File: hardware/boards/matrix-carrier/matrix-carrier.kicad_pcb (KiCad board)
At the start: 2 copper layers, 46.4 x 42 mm, 6 parts, among them J1 2x12 1.27mm shrouded box head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, J2 1x10 2.54mm pin header, SMD, J3 1x10 2.54mm pin header, SMD

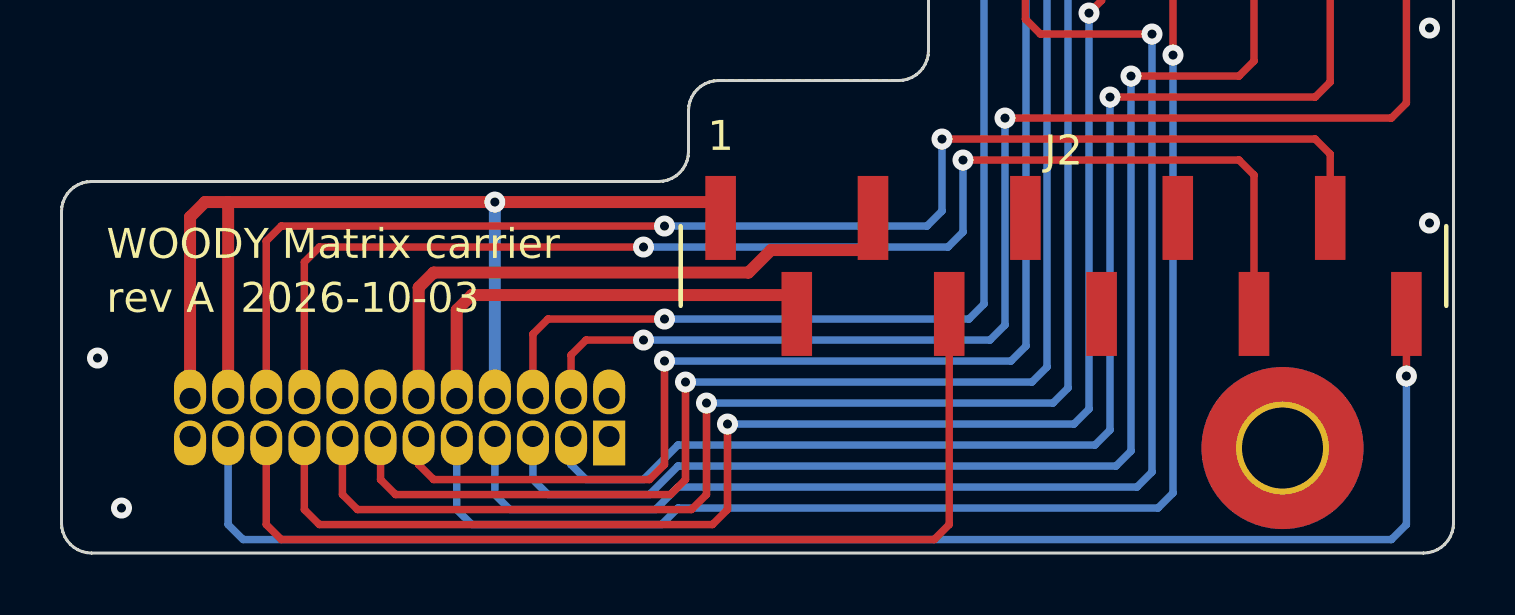
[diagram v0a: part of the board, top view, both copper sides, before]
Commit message: Clash fixes: the Matrix's underside parts drawn at their depth over the carrier (the receptacle is its own solid); the carrier's arm stops short of the right-hand key board's tail end. Carrier re-made on the new outline, check 0 errors, rendered (#23)
Gate-Red: WIP - CAD outputs and clash rebuilding after the scad fix

Co-Authored-By: Claude Opus 5.5 <noreply@anthropic.com>
Claude-Session: https://claude.ai/code/session_01LmB4muFXnoLprWX4JzuJ5A
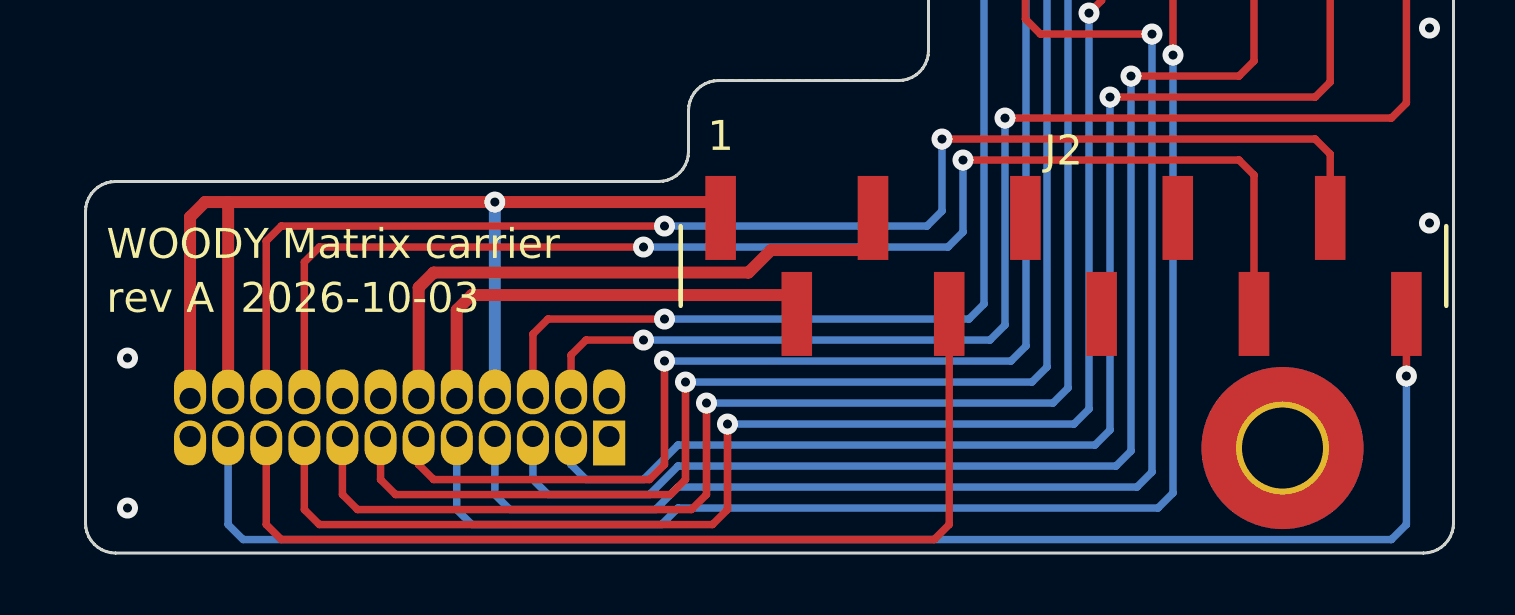
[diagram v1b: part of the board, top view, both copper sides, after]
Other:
- board size 46.4 x 42 mm -> 45.6 x 42 mm

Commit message: #37: MIDI out circuit, the ribbon's MIDI pair, carrier re-route, ADR 0015 amendment
- hardware/carrier/midi-out/: new circuit (sheet, netlist, BOM, page): CA-033's 5 V row
  from U-LVLSHIFT gates B/C, R-MIDI 220R, FB-MIDI, U-TVS-MIDI, J-MIDI (JST PH SMD),
  J-MIDI-OUT (SJ5-43502PM, panel-mount, no footprint), CBL-MIDI. TRS Type A/B in firmware.
- led-strip-drive: gates B/C drive tip/ring; R-MIDI-PU-T/R 10k to DEV_3V3 (power-on default).
- carrier: IO6 on J-MCU 23 (tip) and IO2 on J-MCU 5 (ring) become ports. J-MCU 24 stays
  unconnected: on the Matrix carrier J-MCU-C pin 1 is boxed in by the hand-routed bus.
- matrix-carrier: IO6 routed J-MCU-C pin 2 -> J2.5 (carrier_routes.py); pcb.py check 0 errors.
- main-board root sheet places midi-out; nets.yaml; BOM fragments; CBL-USB-EXT leaves unplaced.csv.
- tools/merge-bom.py: the new fragment added to ORDER (the tool refuses to write when a
  fragment is not listed); no check changed.
- ADR 0015 amendment, ADR 0012 note, firmware/README.md (config mode/OTA deferred; MIDI out),
  draft design in docs/research/.

Gate-Red: pre-existing at 18d0b5f - 37 stale CAD outputs and kicad 131 problems (main-board/module-main PCB parity and clearance). Also red from this checkpoint: the main board's .kicad_pcb is #35's and is not touched, so J-MIDI, R-MIDI-T/R, FB-MIDI-T/R, U-TVS-MIDI, R-MIDI-PU-T/R are unplaced on it and its parity, renders and fab are stale; the CAD and body.yaml changes and the four other stale sims follow in the next commit.

Co-Authored-By: Claude Opus 5.5 <noreply@anthropic.com>
Claude-Session: https://claude.ai/code/session_01LmB4muFXnoLprWX4JzuJ5A
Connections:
- J1 pad 2: unconnected-(J1-Pin_2-Pad2) -> /IO6
- J2 pad 5: unconnected-(J2-Pin_5-Pad5) -> /IO6
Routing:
- net /IO6: track 0.00 -> 20.3 mm, vias 0 -> 1
